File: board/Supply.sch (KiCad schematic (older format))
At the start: 17 parts, among them IC2 AP65101, IC3 AP65101

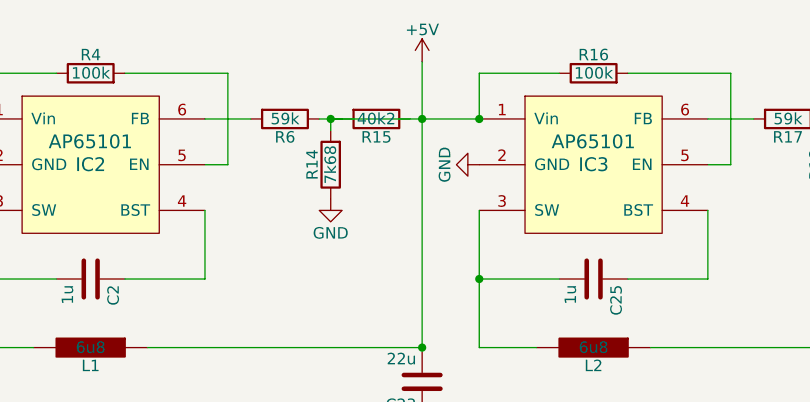
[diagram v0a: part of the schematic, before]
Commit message: - updated layout with recent changes in schematic
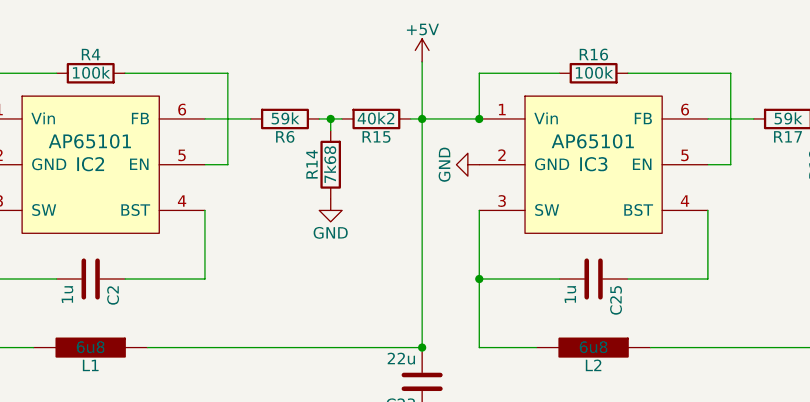
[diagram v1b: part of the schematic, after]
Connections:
- net +5V: now also R15.1; no longer R14.2, R15.2, R6.1
- new net: R14.2, R15.2, R6.1
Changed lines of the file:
@@
 $EndComp
-Wire Wire Line
-	5450 3000 6100 3000
 Wire Wire Line
 	5850 2750 5850 4000
@@
 	1    0    0    -1
 $EndComp
+Wire Wire Line
+	6100 3000 5800 3000
 $EndSCHEMATC

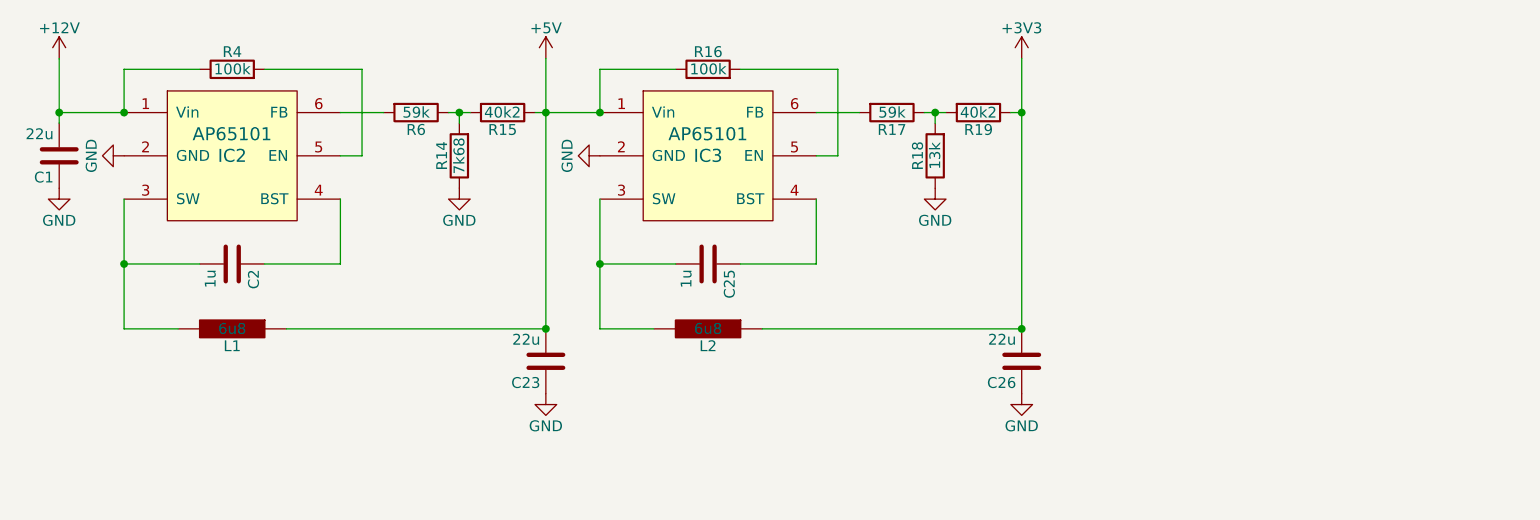
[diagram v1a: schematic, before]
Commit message: - CAN interface isolation
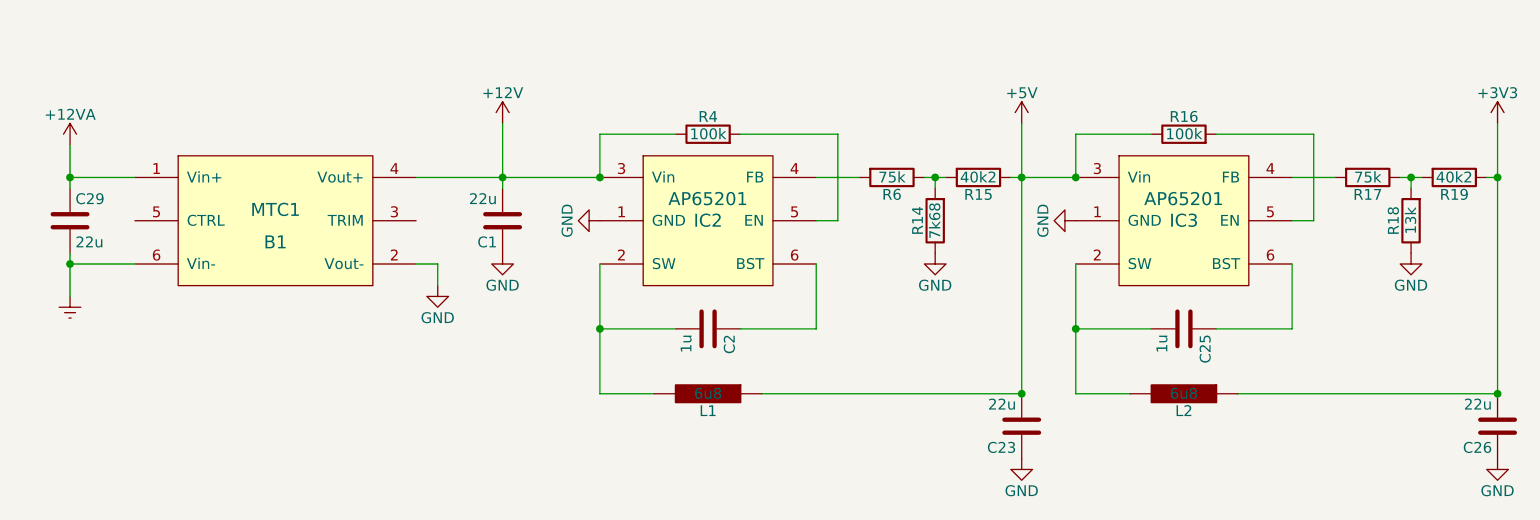
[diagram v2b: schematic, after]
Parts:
- removed IC2, IC3: AP65101, TO_SOT_Packages_SMD:SOT-23-6, symbol AP65101
- added B1: MTC1, alexmod:MTC1, symbol MTC1
- added C29: 22u, Capacitors_SMD:C_0805, symbol C
- added IC2, IC3: AP65201, TO_SOT_Packages_SMD:SOT-23-6, symbol AP65201
- R17, R6: value 59k -> 75k
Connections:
- net +12V: now also B1.4 (Vout+), IC2.3 (Vin)
- net +5V: now also IC3.3 (Vin)
- net GND: now also B1.2 (Vout-), IC2.1 (GND), IC3.1 (GND)
- net at C2.2, L1.2: now also IC2.2 (SW)
- net at C2.1: now also IC2.6 (BST)
- net at R4.2: now also IC2.5 (EN)
- net at R6.2: now also IC2.4 (FB)
- net at C25.2, L2.2: now also IC3.2 (SW)
- net at C25.1: now also IC3.6 (BST)
- net at R16.2: now also IC3.5 (EN)
- net at R17.2: now also IC3.4 (FB)
- new net +12VA: B1.1 (Vin+), C29.1
- new net Earth: B1.6 (Vin-), C29.2
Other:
- moved on the sheet: C1, C2, C23, C25, C26, L1, L2, R14, R15, R16, R17, R18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
